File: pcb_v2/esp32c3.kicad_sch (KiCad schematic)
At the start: 34 parts, among them J6 Conn_01x03_Pin, Q1 2N7002, Q2 2N7002, Q3 2N7002, Q4 2N7002, Q5 2N7002, Q6 2N7002, SW1 SW_Push, U3 ESP32-C3-WROOM-02, Y1 32K

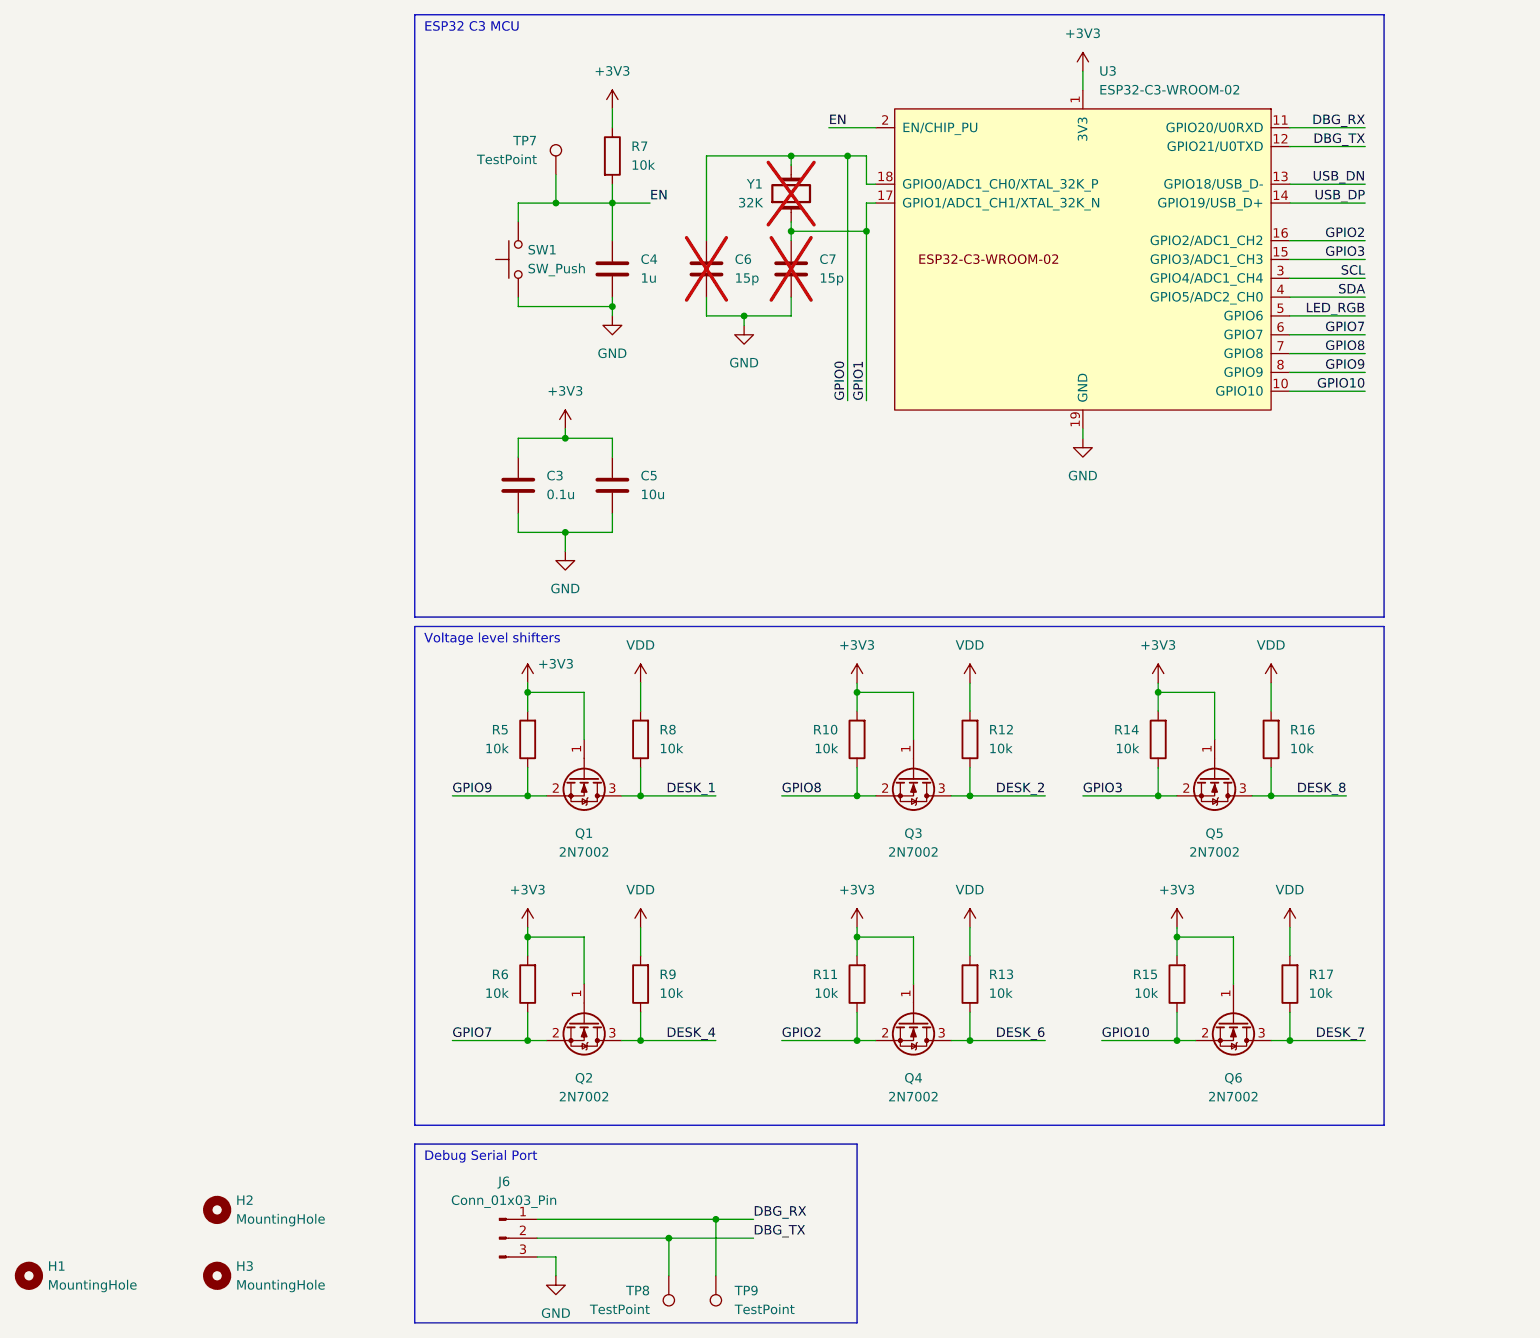
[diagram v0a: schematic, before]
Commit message: Connect pin sheets. Add protection on USB. Use SolderJumpers.
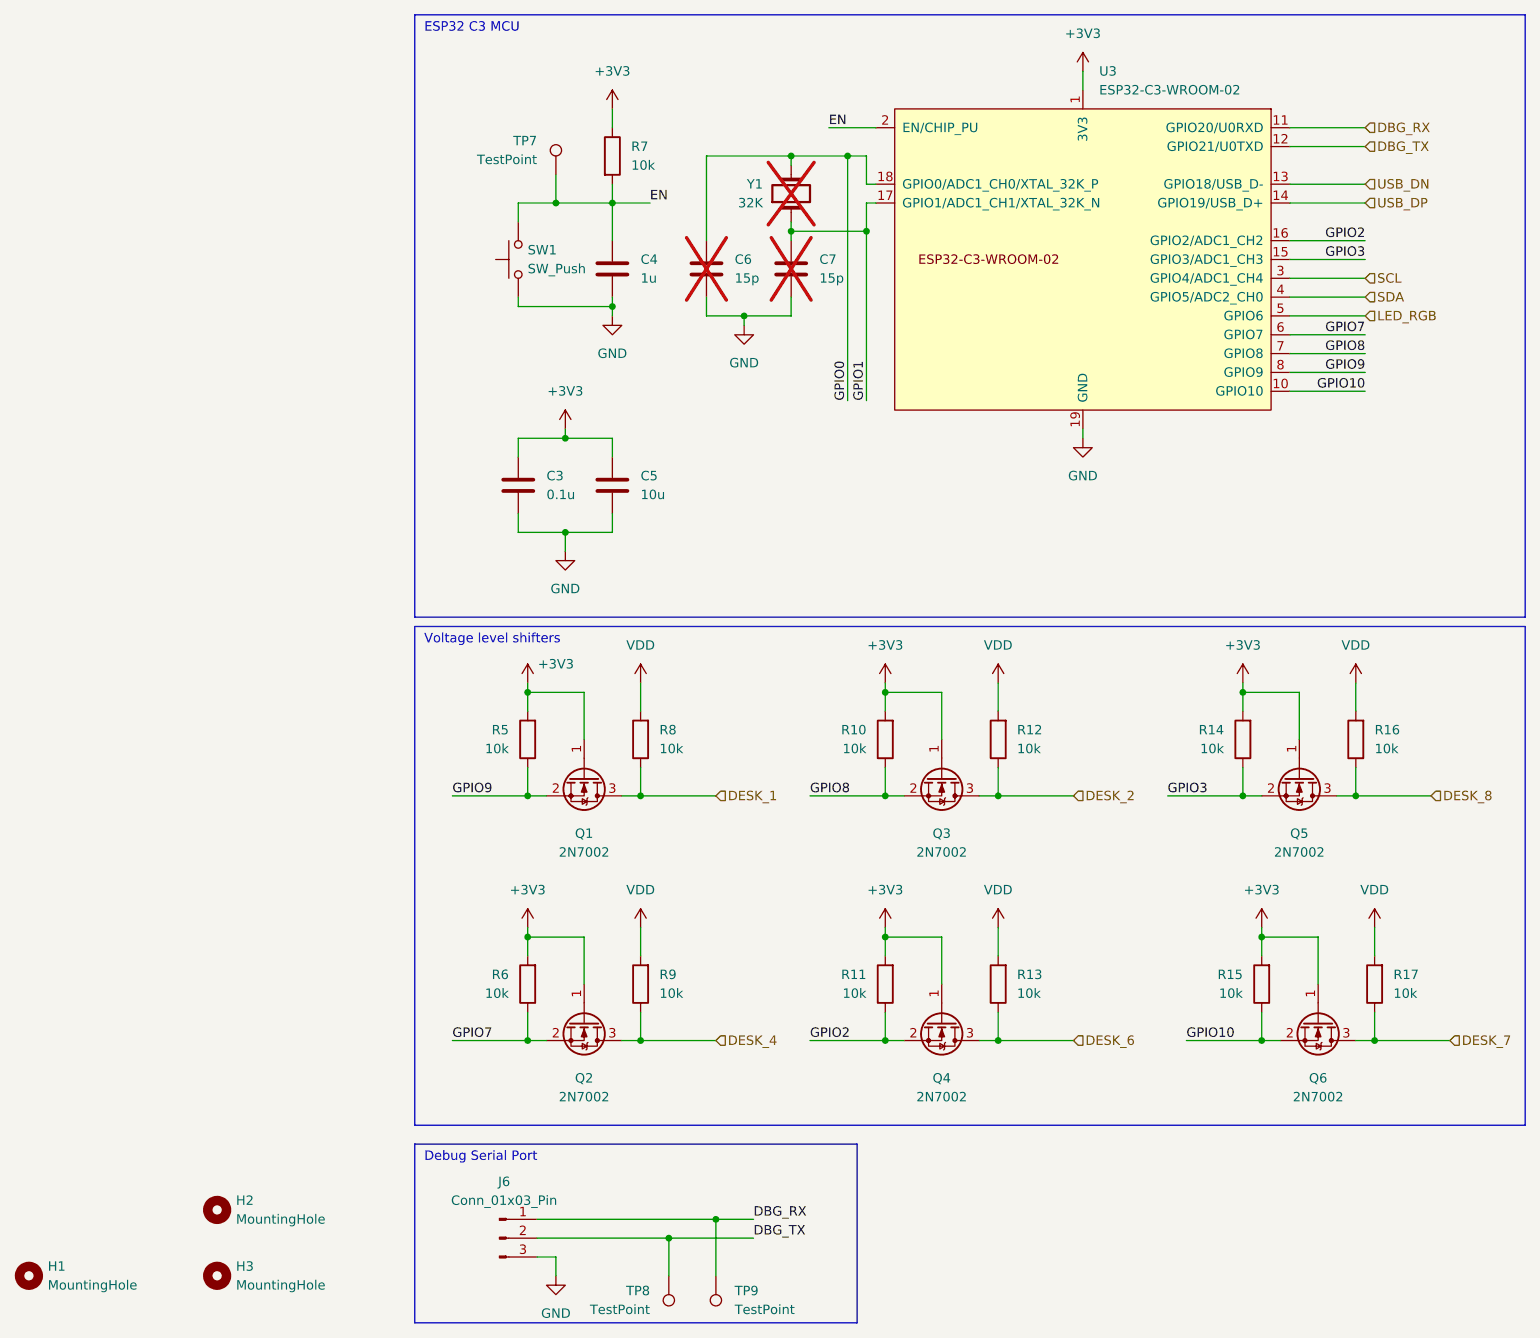
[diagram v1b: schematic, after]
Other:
- moved on the sheet: Q3, Q4, Q5, Q6, R10, R11, R12, R13, R14, R15, R16, R17
